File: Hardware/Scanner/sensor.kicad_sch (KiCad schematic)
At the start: 23 parts, among them U1 OPA2376xxD, U4 OPA2376xxD

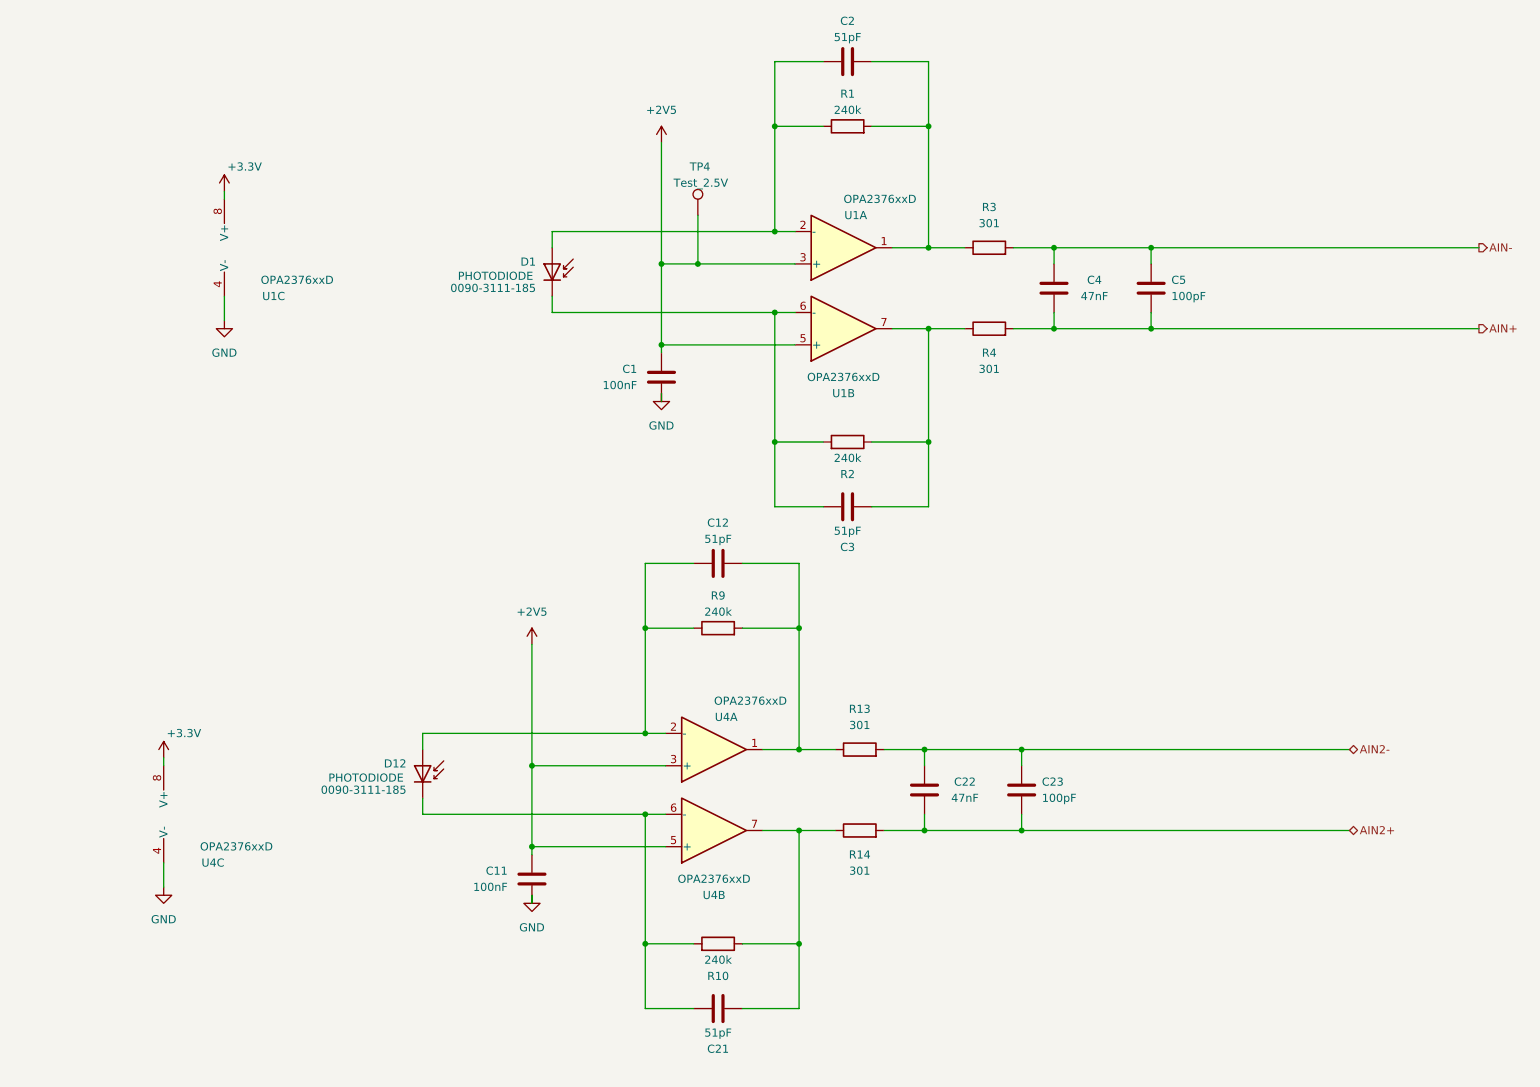
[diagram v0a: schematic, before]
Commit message: added footprint for MTSM2601SMF1-100
Signed-off-by: lokimetasmith <lokimail@gmail.com>
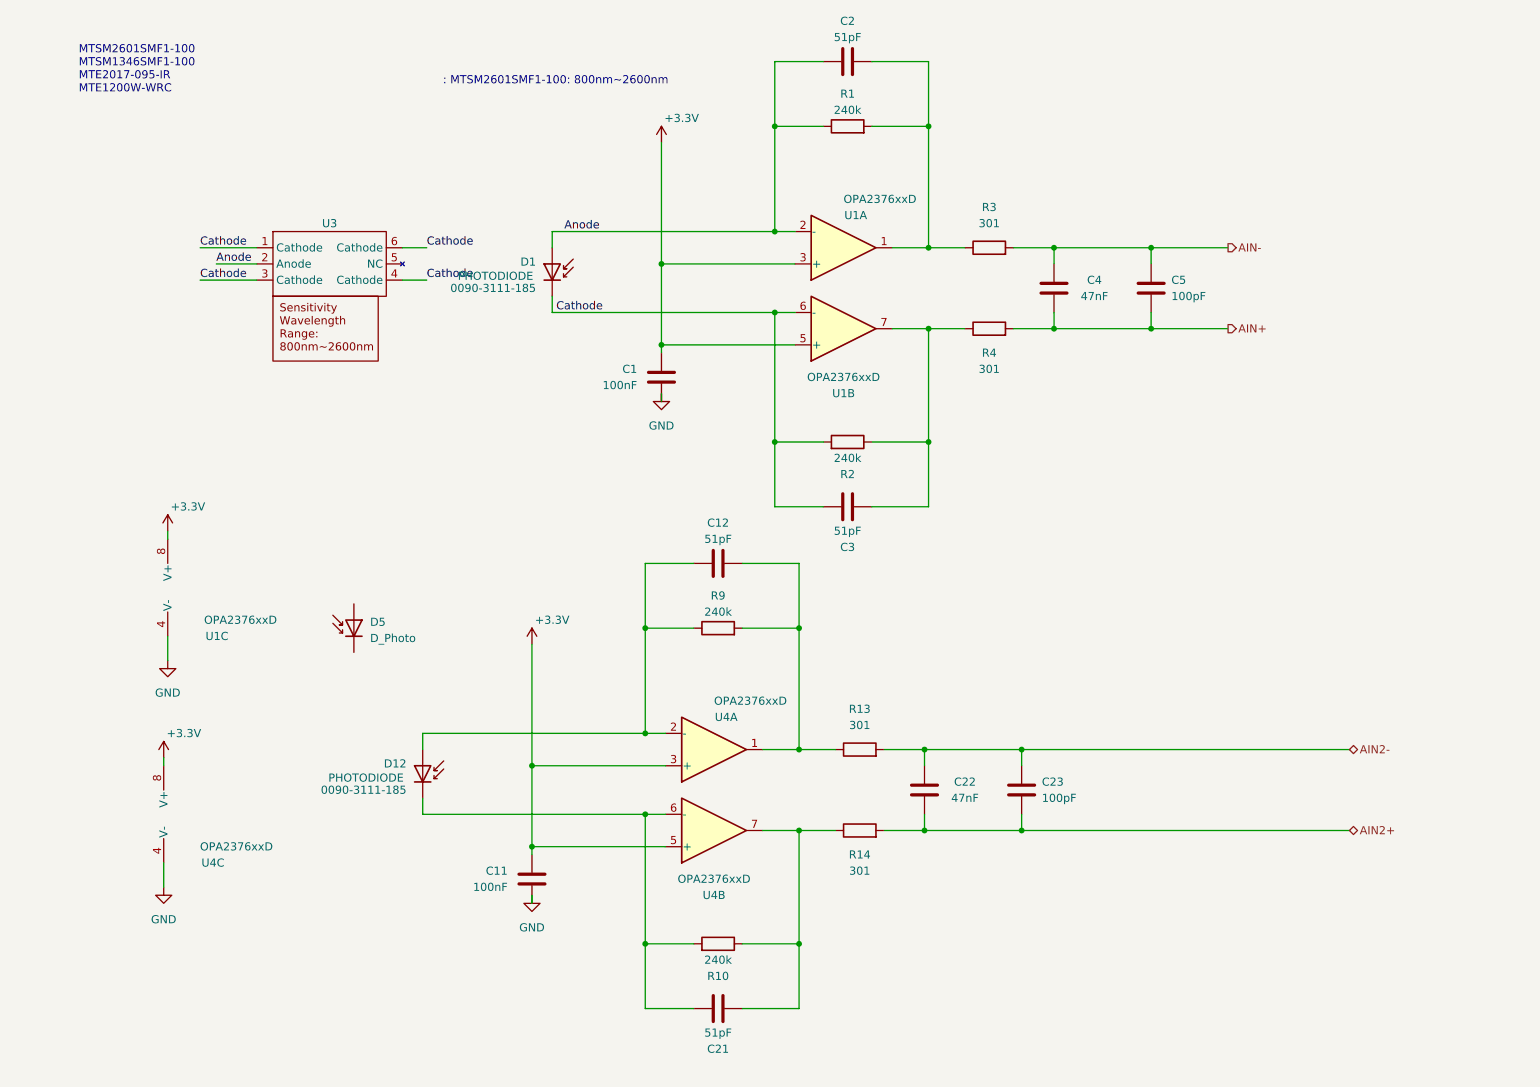
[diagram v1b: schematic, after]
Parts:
- removed TP4: Test_2.5V, TestPoint:TestPoint_Pad_D1.5mm, symbol Connector:TestPoint
- added D5: D_Photo, symbol Device:D_Photo
- added U3: ~, MTSM2601SMF1-100:MTSM2601SMF1-100, symbol MTSM2601SMF1-100:MTSM2601SMF1-100
- U1, U4: digikey part number (none) -> 296-26263-5-ND
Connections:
- net +2V5 is gone; now on net +3V3: C1.2, C11.2, U1.3 (+), U1.5 (+), U4.3 (+), U4.5 (+)
- net Cathode: now reaches C3.1, D1.1 (K), R2.2, U1.6 (-)
- net Cathode: now also U3.1 (Cathode), U3.3 (Cathode), U3.4 (Cathode), U3.6 (Cathode)
- net Anode: now reaches C2.1, D1.2 (A), R1.1, U1.2 (-)
- net Anode: now also U3.2 (Anode)
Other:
- note added: ": MTSM2601SMF1-100: 800nm~2600nm"
- note added: "MTSM2601SMF1-100 MTSM1346SMF1-100 MTE2017-095-IR MTE1200W-WRC"
- moved on the sheet: U1C

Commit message: lots of changes, added footprints, fixed broken schemaitcs, fixed kicad 7.0 issues
Signed-off-by: lokimetasmith <lokimail@gmail.com>
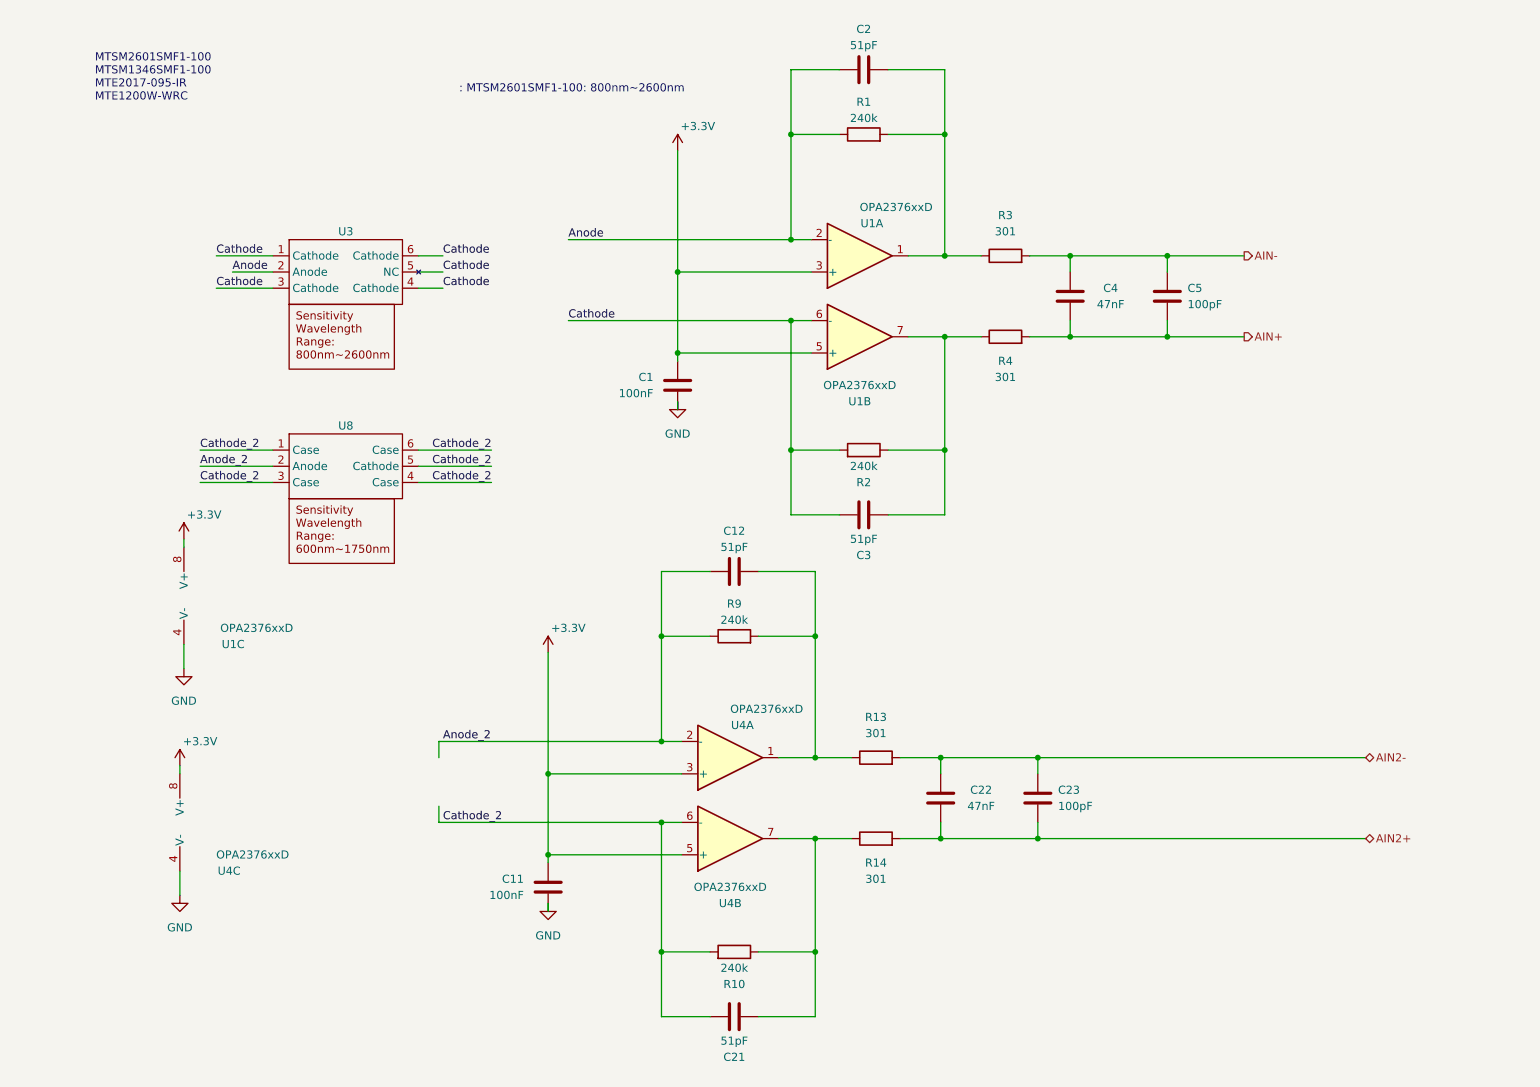
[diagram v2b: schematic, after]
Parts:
- removed D1, D12: 0090-3111-185, Diode_SMD:D_1206_3216Metric_Pad1.42x1.75mm_HandSolder, symbol Device:D_Photo
- removed D5: D_Photo, symbol Device:D_Photo
- added U8: ~, MTSM2601SMF1-100:MTSM1346SMF1-100, symbol MTSM2601SMF1-100:MTSM1346SMF1-100
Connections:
- net Cathode: now also U3.5 (NC)
- net Anode_2: now reaches C12.1, R9.1, U4.2 (-)
- net Anode_2: now also U8.2 (Anode)
- net Cathode_2: now reaches C21.1, R10.2, U4.6 (-)
- net Cathode_2: now also U8.1 (Case), U8.3 (Case), U8.4 (Case), U8.5 (Cathode), U8.6 (Case)
- net +3V3 renamed +3.3V
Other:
- moved on the sheet: C1, C11, C12, C2, C21, C22, C23, C3, C4, C5, R1, R10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

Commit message: added linear regulator for reference voltage
Signed-off-by: lokimetasmith <lokimail@gmail.com>
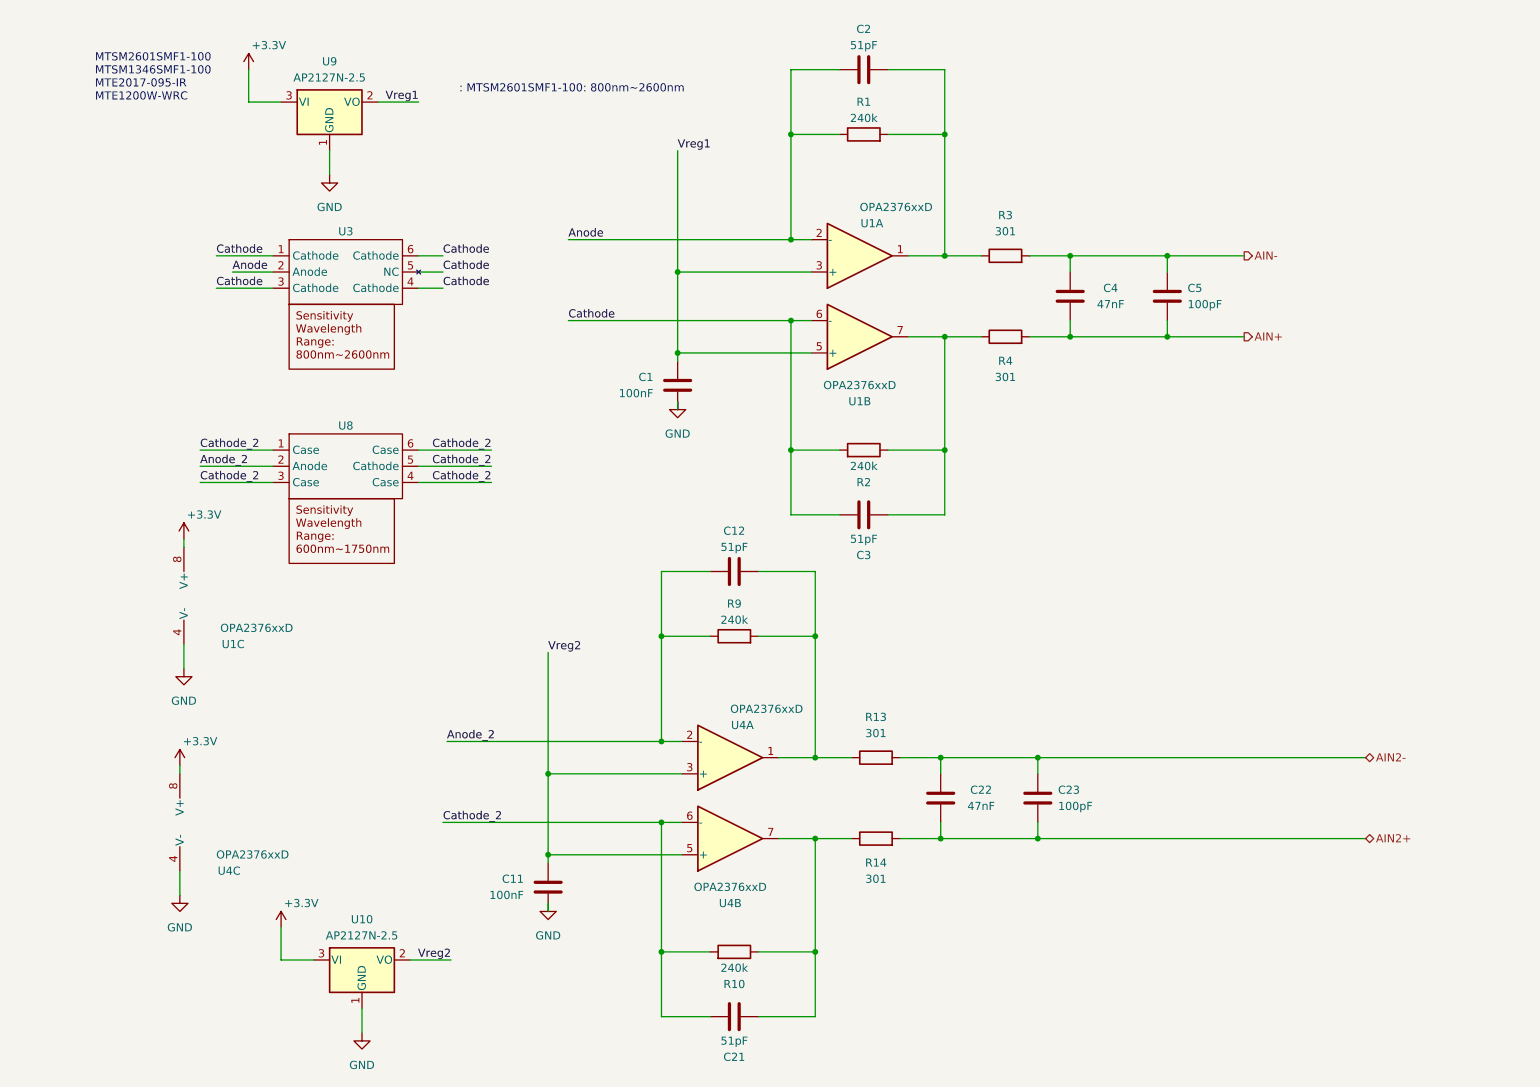
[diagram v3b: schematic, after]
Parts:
- added U10, U9: AP2127N-2.5, Package_TO_SOT_SMD:SOT-23, symbol Regulator_Linear:AP2127N-2.5
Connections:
- net +3.3V: now also U10.3 (VI), U9.3 (VI); no longer C1.2, C11.2, U1.3 (+), U1.5 (+), U4.3 (+), U4.5 (+)
- net GND: now also U10.1 (GND), U9.1 (GND)
- new net Vreg1: C1.2, U1.3 (+), U1.5 (+), U9.2 (VO)
- new net Vreg2: C11.2, U10.2 (VO), U4.3 (+), U4.5 (+)

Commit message: added options for using internal adc, external adc, or 3.3v
Signed-off-by: lokimetasmith <lokimail@gmail.com>
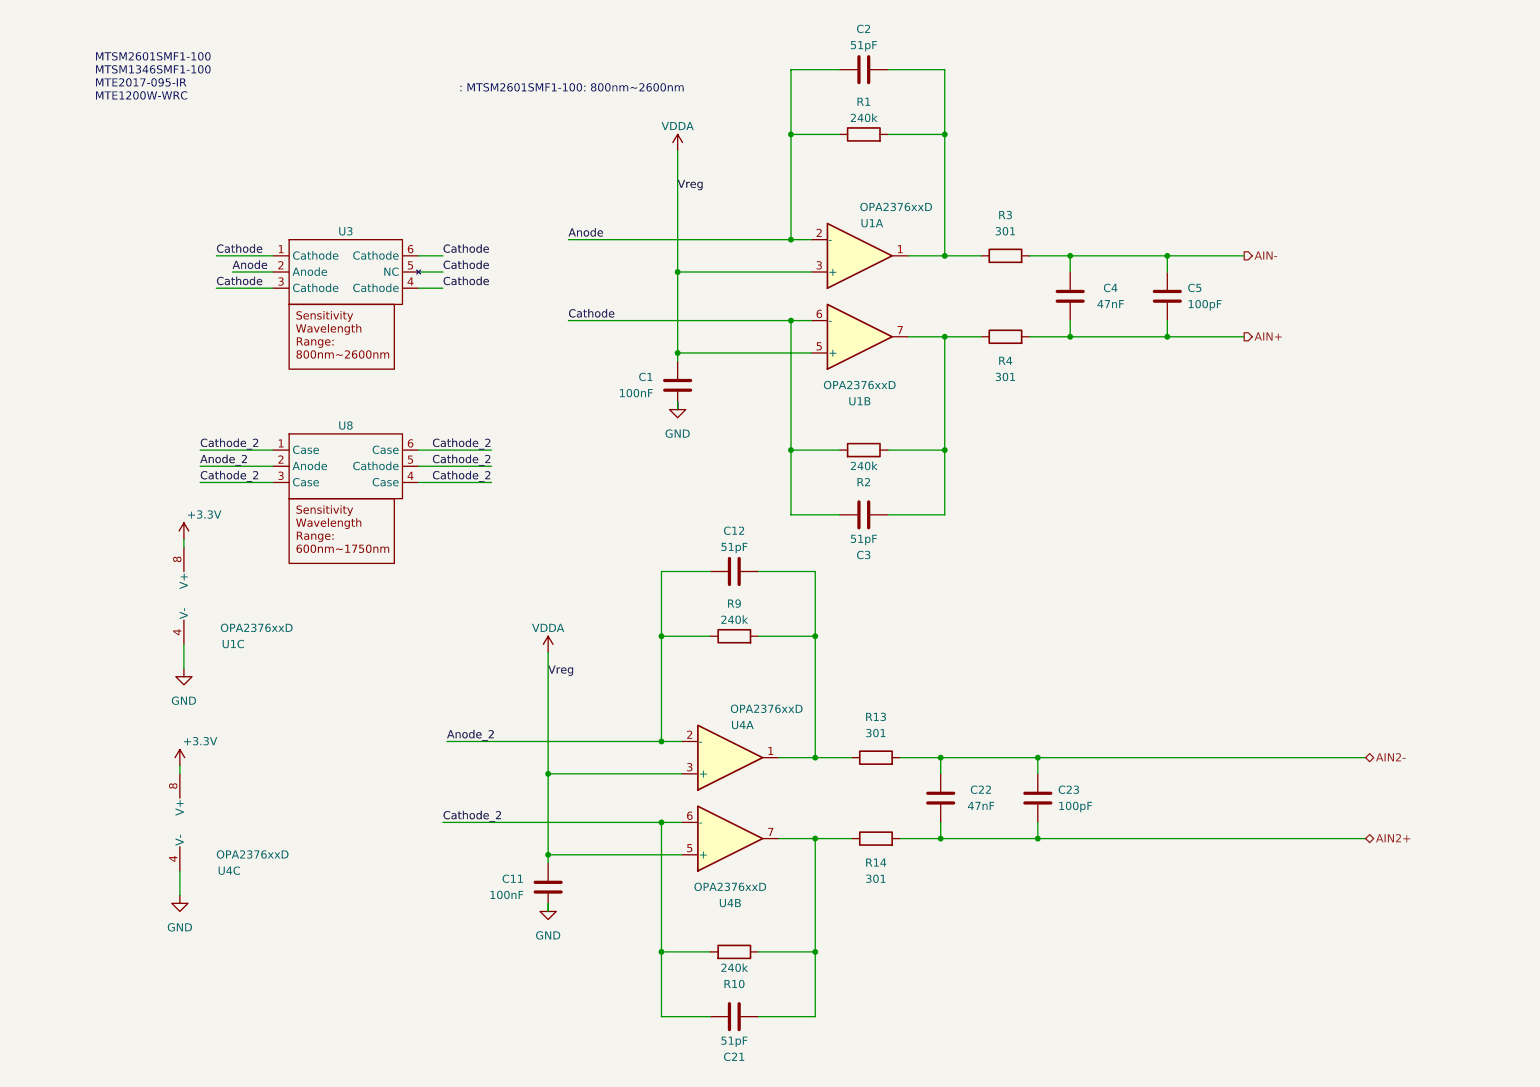
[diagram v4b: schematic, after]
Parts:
- removed U10, U9: AP2127N-2.5, Package_TO_SOT_SMD:SOT-23, symbol Regulator_Linear:AP2127N-2.5
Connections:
- net Vreg2 is gone; now on net VDDA: C11.2, U4.3 (+), U4.5 (+)
- net Vreg1 renamed VDDA
